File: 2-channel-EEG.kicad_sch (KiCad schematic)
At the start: 3 parts, among them U1 AD8237

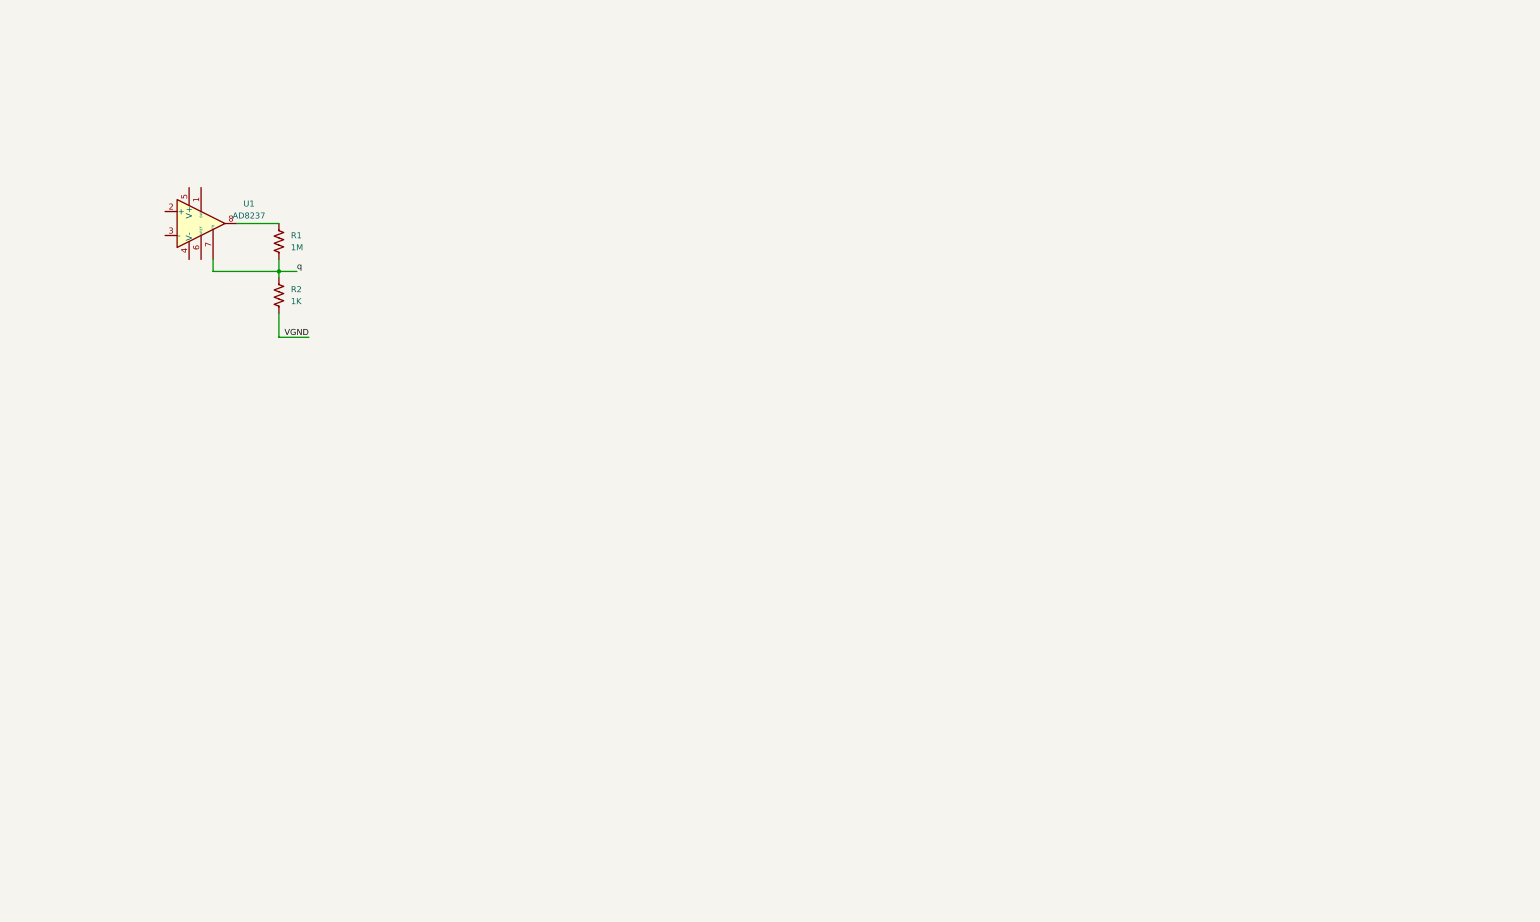
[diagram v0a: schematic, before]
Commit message: Schematic Updates
isolation converter, 3.3V LDO, Channel1, Driven GND, Rail Splitter
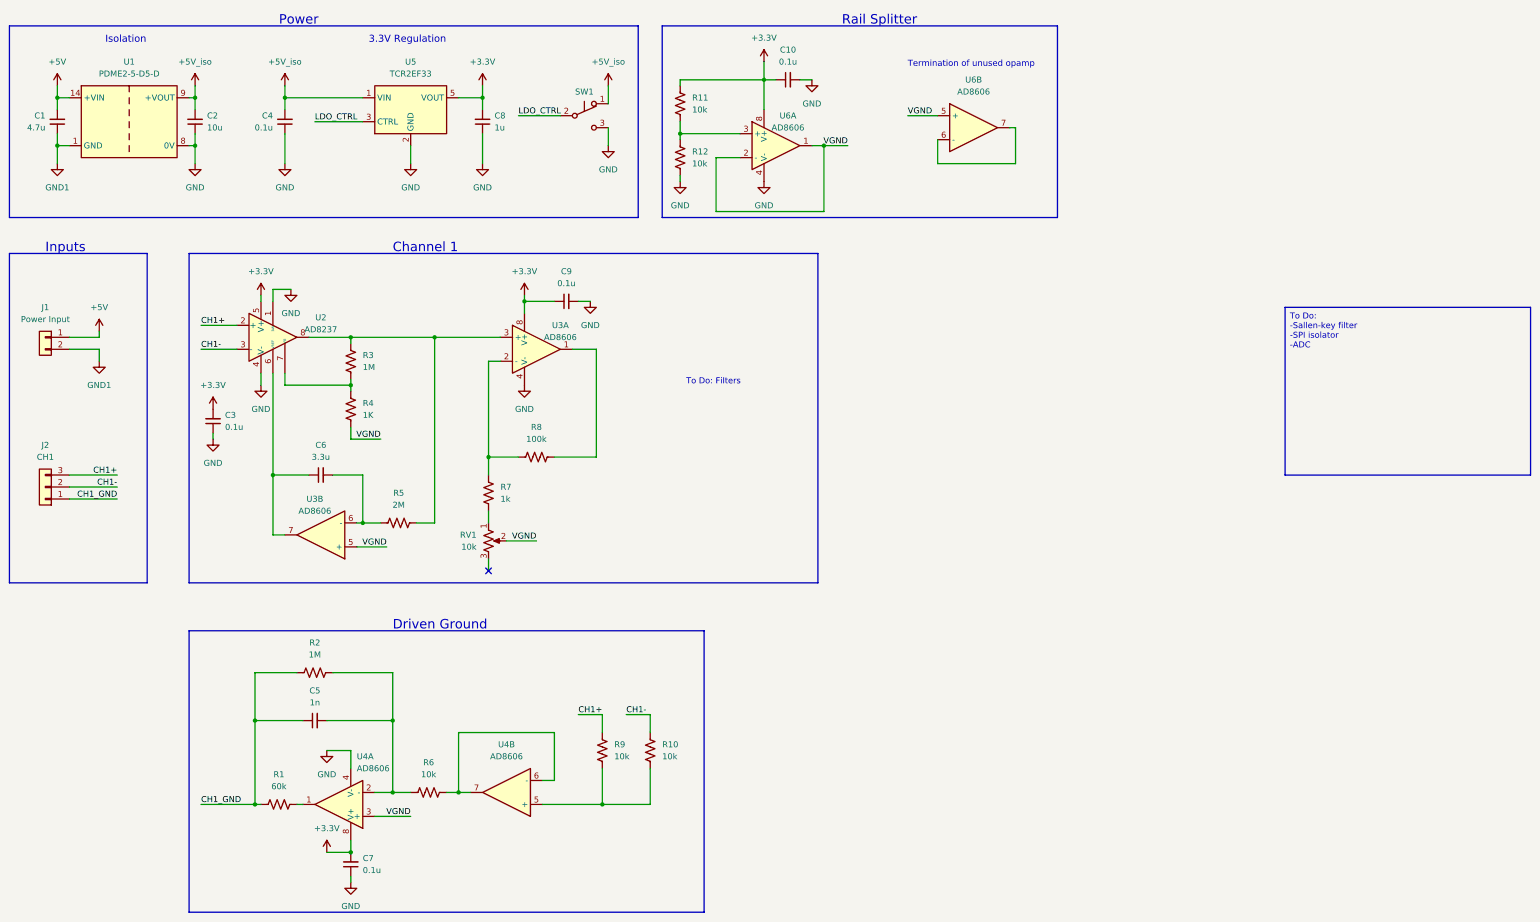
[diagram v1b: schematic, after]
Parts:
- added C1: 4.7u, symbol Device:C_Small
- added C10, C3, C4, C7, C9: 0.1u, symbol Device:C_Small
- added C2: 10u, symbol Device:C_Small
- added C5: 1n, symbol Device:C_Small
- added C6: 3.3u, symbol Device:C_Small
- added C8: 1u, symbol Device:C_Small
- added J1: Power Input, symbol Connector_Generic:Conn_01x02
- added J2: CH1, symbol Connector_Generic:Conn_01x03
- added R1: 60k, symbol Device:R_US
- added R10, R11, R12, R6, R9: 10k, symbol Device:R_US
- added R2: 1M, symbol Device:R_US
- added R5: 2M, symbol Device:R_US
- added R7: 1k, symbol Device:R_US
- added R8: 100k, symbol Device:R_US
- added RV1: 10k, symbol Device:R_Potentiometer_US
- added SW1: SW_Push_SPDT, symbol Switch:SW_Push_SPDT
- added U1: PDME2-5-D5-D, symbol Senior_Project_Library:PDME2-5-D5-D
- added U3, U4, U6: AD8606, symbol Senior_Project_Library:AD8606
- added U5: TCR2EF33, Package_TO_SOT_SMD:SOT-553, symbol Senior_Project_Library:TCR2EF33
- renumbered R1 to R3, R2 to R4, U1 to U2
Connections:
- net VGND: now also RV1.2, U3.5 (+), U4.3 (+), U6.1, U6.2 (-), U6.5 (+)
- net GND: now reaches U2.1 (BW)
- net GND: now also U2.4 (V-), C10.2, C2.1, C3.1, C4.1, C7.1, C8.1, C9.2, R12.1, SW1.3 (C), U1.8 (0V), U3.4 (V-), U4.4 (V-), U5.2 (GND), U6.4 (V-)
- net CH1+: now reaches U2.2 (+)
- net CH1+: now also J2.3 (Pin_3), R9.2
- net CH1-: now reaches U2.3 (-)
- net CH1-: now also J2.2 (Pin_2), R10.2
- net +3.3V: now reaches U2.5 (V+)
- net +3.3V: now also C10.1, C2.2, C3.2, C4.2, C7.2, C8.2, C9.1, R11.2, SW1.1 (A), U1.9 (+VOUT), U3.8 (V+), U4.8 (V+), U5.1 (VIN), U5.5 (VOUT), U6.8 (V+)
- net at U2.6 (VREF): now also C6.1, U3.7
- net at R3.1, U2.8: now also R5.2, U3.3 (+)
- net q: no longer names the net of R3.2, R4.1, U2.7 (FB)
- new net: C5.2, R2.2, R6.1, U4.2 (-)
- new net: R6.2, U4.6 (-), U4.7
- new net: R11.1, R12.2, U6.3 (+)
- new net: C6.2, R5.1, U3.6 (-)
- new net: R7.1, RV1.1
- new net: R7.2, R8.1, U3.2 (-)
- new net: R1.2, U4.1
- new net: R8.2, U3.1
- new net: R10.1, R9.1, U4.5 (+)
- new net: U6.6 (-), U6.7
- new net +5V: C1.2, J1.1 (Pin_1), U1.14 (+VIN)
- new net CH1_GND: C5.1, J2.1 (Pin_1), R1.1, R2.1
- new net GND1: C1.1, J1.2 (Pin_2), U1.1 (GND)
- new net LDO_CTRL: SW1.2 (B), U5.3 (CTRL)
- no-connect marks 0 -> 1
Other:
- note added: "3.3V Regulation"
- note added: "Channel 1"
- note added: "Driven Ground"
- note added: "Inputs"
- note added: "Isolation"
- note added: "Power"
- note added: "Rail Splitter"
- note added: "Termination of unused opamp"
- note added: "To Do: Filters"
- moved on the sheet: R3, R4, U2
